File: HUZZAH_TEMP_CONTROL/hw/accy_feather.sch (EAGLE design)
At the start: 10 parts, among them K1 G6RS

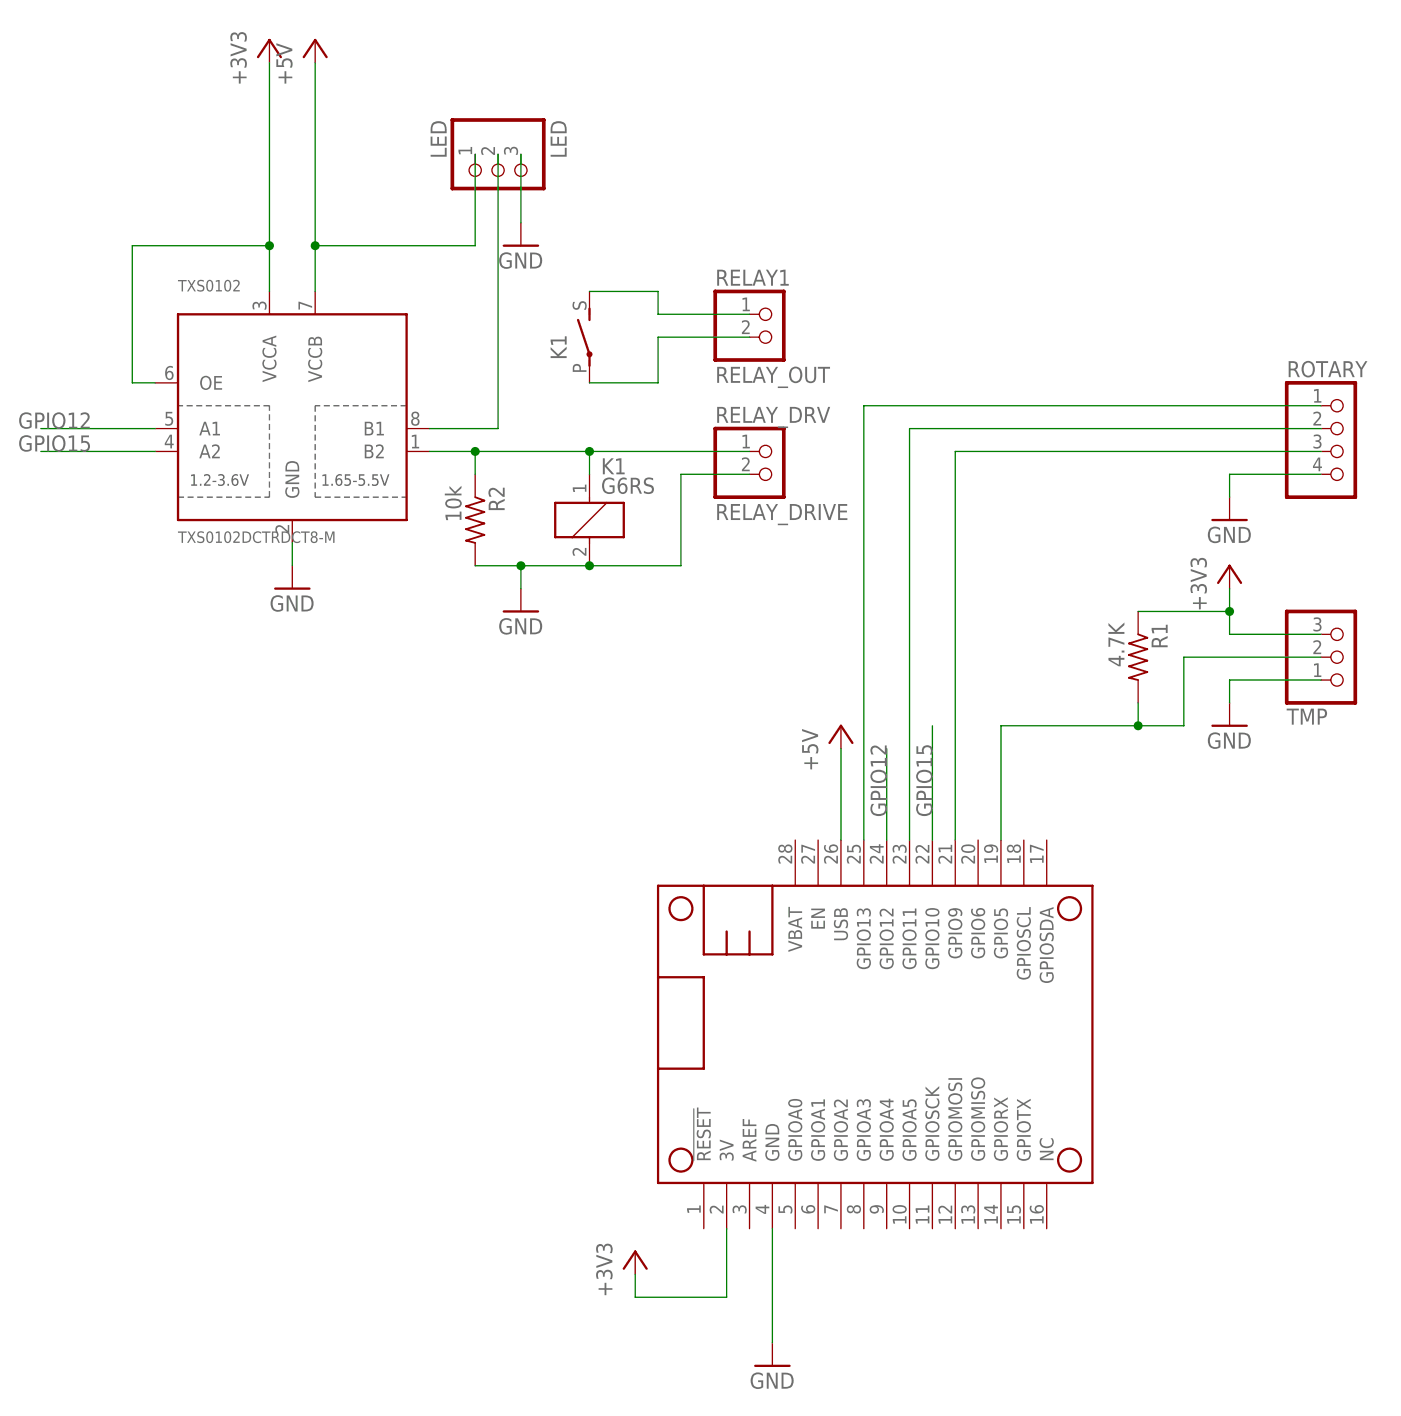
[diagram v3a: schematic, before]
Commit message: Accessory board version 2.1
Moved relay to a transistor based 1-way level shifter.  The
2-way level shifter was causing problems with boot mode pins.
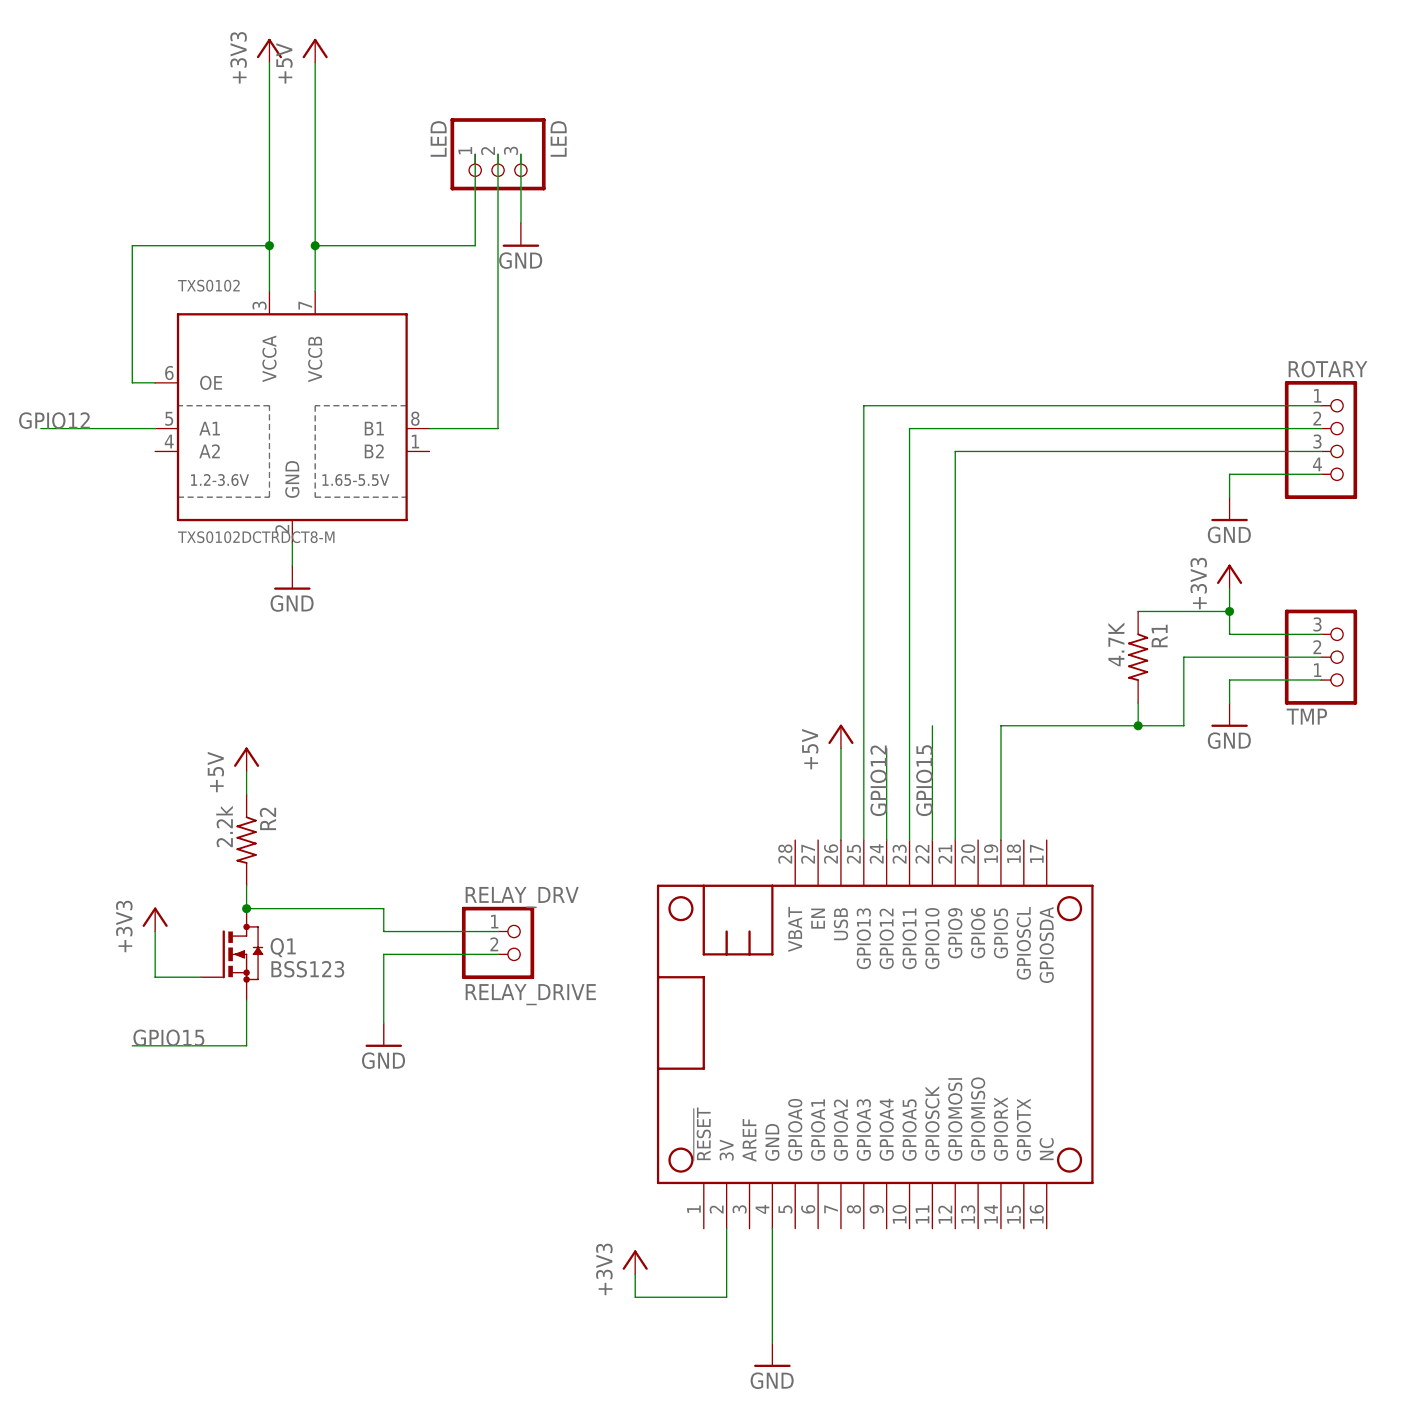
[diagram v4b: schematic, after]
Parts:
- removed K1: G6RS, relay:G6RS
- removed RELAY1: RELAY_OUT, pinhead:PINHD-1X2
- added Q1: BSS123, transistor-small-signal:BSS123
- R2: value 10k -> 2.2k
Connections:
- removed net N$2: K12.P, RELAY1.2
- removed net RELAY: K11.1, R2.1, RELAY_DRV.1, TXS0102.B2
- removed net RELAY_CTRL: K12.S, RELAY1.1
- new net N$1: Q1.D, R2.2, RELAY_DRV.1
- net +3V3: now also Q1.G
- net +5V: now also R2.1
- net GND: no longer K11.2, R2.2
- net GPIO15: now also Q1.S; no longer TXS0102.A2
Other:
- moved on the sheet: R2, RELAY_DRV
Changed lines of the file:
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@@
 <part name="ROTARY" library="pinhead" deviceset="PINHD-1X4" device=""/>
 <part name="TXS0102" library="DZ" deviceset="TXS0102DCTR" device="DCT8-M"/>
-<part name="R2" library="resistor" deviceset="R-US_" device="R0603" value="10k"/>
-<part name="K1" library="relay" deviceset="G6RS" device=""/>
-<part name="RELAY1" library="pinhead" deviceset="PINHD-1X2" device="" value="RELAY_OUT"/>
+<part name="Q1" library="transistor-small-signal" deviceset="BSS123" device=""/>
+<part name="R2" library="resistor" deviceset="R-US_" device="R0603" value="2.2k"/>
+<part name="P+3" library="supply1" deviceset="+5V" device=""/>
+<part name="+3V4" library="supply1" deviceset="+3V3" device=""/>
 </parts>
 <sheets>
@@
 <instance part="LED" gate="A" x="58.42" y="157.48" rot="MR270"/>
 <instance part="GND6" gate="1" x="139.7" y="119.38"/>
-<instance part="GND3" gate="1" x="60.96" y="109.22"/>
-<instance part="RELAY_DRV" gate="G$1" x="88.9" y="124.46"/>
+<instance part="GND3" gate="1" x="45.72" y="60.96"/>
+<instance part="RELAY_DRV" gate="G$1" x="60.96" y="71.12"/>
 <instance part="ROTARY" gate="A" x="152.4" y="127"/>
 <instance part="TXS0102" gate="A" x="22.86" y="119.38"/>
-<instance part="R2" gate="G$1" x="55.88" y="119.38" rot="R270"/>
-<instance part="K1" gate="1" x="68.58" y="119.38"/>
-<instance part="K1" gate="2" x="68.58" y="139.7"/>
-<instance part="RELAY1" gate="G$1" x="88.9" y="139.7"/>
+<instance part="Q1" gate="G$1" x="30.48" y="71.12"/>
+<instance part="R2" gate="G$1" x="30.48" y="83.82" rot="R270"/>
+<instance part="P+3" gate="1" x="30.48" y="93.98"/>
+<instance part="+3V4" gate="G$1" x="20.32" y="76.2"/>
 </instances>
 <busses>
@@
 </segment>
 <segment>
+<pinref part="RELAY_DRV" gate="G$1" pin="2"/>
+<wire x1="58.42" y1="71.12" x2="45.72" y2="71.12" width="0.1524" layer="91"/>
 <pinref part="GND3" gate="1" pin="GND"/>
-<wire x1="60.96" y1="114.3" x2="60.96" y2="111.76" width="0.1524" layer="91"/>
-<pinref part="R2" gate="G$1" pin="2"/>
-<wire x1="55.88" y1="114.3" x2="60.96" y2="114.3" width="0.1524" layer="91"/>
-<pinref part="RELAY_DRV" gate="G$1" pin="2"/>
-<wire x1="86.36" y1="124.46" x2="78.74" y2="124.46" width="0.1524" layer="91"/>
-<wire x1="78.74" y1="124.46" x2="78.74" y2="114.3" width="0.1524" layer="91"/>
-<wire x1="78.74" y1="114.3" x2="68.58" y2="114.3" width="0.1524" layer="91"/>
-<pinref part="K1" gate="1" pin="2"/>
-<wire x1="68.58" y1="114.3" x2="60.96" y2="114.3" width="0.1524" layer="91"/>
-<junction x="68.58" y="114.3"/>
-<junction x="60.96" y="114.3"/>
+<wire x1="45.72" y1="71.12" x2="45.72" y2="63.5" width="0.1524" layer="91"/>
 </segment>
 </net>
@@
 <junction x="38.1" y="149.86"/>
 <pinref part="TXS0102" gate="A" pin="VCCB"/>
+</segment>
+<segment>
+<pinref part="R2" gate="G$1" pin="1"/>
+<pinref part="P+3" gate="1" pin="+5V"/>
+<wire x1="30.48" y1="88.9" x2="30.48" y2="91.44" width="0.1524" layer="91"/>
 </segment>
 </net>
@@
 <net name="GPIO15" class="0">
 <segment>
-<wire x1="20.32" y1="127" x2="7.62" y2="127" width="0.1524" layer="91"/>
-<label x="5.08" y="127" size="1.778" layer="95"/>
-<pinref part="TXS0102" gate="A" pin="A2"/>
-</segment>
-<segment>
 <pinref part="MS1" gate="G$1" pin="GPIO10"/>
 <wire x1="106.68" y1="83.82" x2="106.68" y2="96.52" width="0.1524" layer="91"/>
 <label x="106.68" y="86.36" size="1.778" layer="95" rot="R90"/>
+</segment>
+<segment>
+<pinref part="Q1" gate="G$1" pin="S"/>
+<wire x1="30.48" y1="66.04" x2="30.48" y2="60.96" width="0.1524" layer="91"/>
+<wire x1="30.48" y1="60.96" x2="17.78" y2="60.96" width="0.1524" layer="91"/>
+<label x="17.78" y="60.96" size="1.778" layer="95"/>
 </segment>
 </net>
@@
 <junction x="139.7" y="109.22"/>
 </segment>
+<segment>
+<pinref part="Q1" gate="G$1" pin="G"/>
+<wire x1="25.4" y1="68.58" x2="20.32" y2="68.58" width="0.1524" layer="91"/>
+<pinref part="+3V4" gate="G$1" pin="+3V3"/>
+<wire x1="20.32" y1="68.58" x2="20.32" y2="73.66" width="0.1524" layer="91"/>
+</segment>
 </net>
 <net name="LED_DATA" class="0">
@@
 </segment>
 </net>
-<net name="RELAY" class="0">
+<net name="N$1" class="0">
 <segment>
 <pinref part="RELAY_DRV" gate="G$1" pin="1"/>
-<wire x1="86.36" y1="127" x2="68.58" y2="127" width="0.1524" layer="91"/>
-<pinref part="TXS0102" gate="A" pin="B2"/>
-<pinref part="R2" gate="G$1" pin="1"/>
-<wire x1="68.58" y1="127" x2="55.88" y2="127" width="0.1524" layer="91"/>
-<wire x1="55.88" y1="127" x2="50.8" y2="127" width="0.1524" layer="91"/>
-<wire x1="55.88" y1="124.46" x2="55.88" y2="127" width="0.1524" layer="91"/>
-<junction x="55.88" y="127"/>
-<pinref part="K1" gate="1" pin="1"/>
-<wire x1="68.58" y1="124.46" x2="68.58" y2="127" width="0.1524" layer="91"/>
-<junction x="68.58" y="127"/>
-</segment>
-</net>
-<net name="N$2" class="0">
-<segment>
-<pinref part="RELAY1" gate="G$1" pin="2"/>
-<wire x1="86.36" y1="139.7" x2="76.2" y2="139.7" width="0.1524" layer="91"/>
-<wire x1="76.2" y1="139.7" x2="76.2" y2="134.62" width="0.1524" layer="91"/>
-<pinref part="K1" gate="2" pin="P"/>
-<wire x1="76.2" y1="134.62" x2="68.58" y2="134.62" width="0.1524" layer="91"/>
-</segment>
-</net>
-<net name="RELAY_CTRL" class="0">
-<segment>
-<pinref part="RELAY1" gate="G$1" pin="1"/>
-<wire x1="86.36" y1="142.24" x2="76.2" y2="142.24" width="0.1524" layer="91"/>
-<wire x1="76.2" y1="142.24" x2="76.2" y2="144.78" width="0.1524" layer="91"/>
-<pinref part="K1" gate="2" pin="S"/>
-<wire x1="76.2" y1="144.78" x2="68.58" y2="144.78" width="0.1524" layer="91"/>
-</segment>
-</net>
+<wire x1="58.42" y1="73.66" x2="45.72" y2="73.66" width="0.1524" layer="91"/>
+<wire x1="45.72" y1="73.66" x2="45.72" y2="76.2" width="0.1524" layer="91"/>
+<pinref part="Q1" gate="G$1" pin="D"/>
+<pinref part="R2" gate="G$1" pin="2"/>
+<wire x1="30.48" y1="76.2" x2="30.48" y2="78.74" width="0.1524" layer="91"/>
+<wire x1="45.72" y1="76.2" x2="30.48" y2="76.2" width="0.1524" layer="91"/>
+<junction x="30.48" y="76.2"/>
+</segment>
+</net>
